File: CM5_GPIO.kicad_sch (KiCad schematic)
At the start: 20 parts, among them J14 JST_SHBM04B-SRSS-TB, J3 Conn_01x03, J7 Micro_SD_Card_Det, J8 THD-20-R, SW1 Right angle Tact button, U18 RT9742GGJ5

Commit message: end of jan 11th
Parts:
- added J2: Conn_02x07_Odd_Even, Connector_PinHeader_2.54mm:PinHeader_2x07_P2.54mm_Vertical, symbol Connector_Generic:Conn_02x07_Odd_Even
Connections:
- net EEPROM_nWP: now also J2.4 (Pin_4)
- net GND: now also J2.1 (Pin_1), J2.11 (Pin_11), J2.13 (Pin_13), J2.3 (Pin_3), J2.5 (Pin_5), J2.7 (Pin_7), J2.9 (Pin_9)
- net PMIC_ENABLE: now also J2.12 (Pin_12)
- net PWR_BUT: now also J2.14 (Pin_14)
- net SYNC_OUT: now also J2.6 (Pin_6)
- net nRPIBOOT: now also J2.2 (Pin_2)
- new net USBOTG: J2.10 (Pin_10)
- no-connect marks 8 -> 20

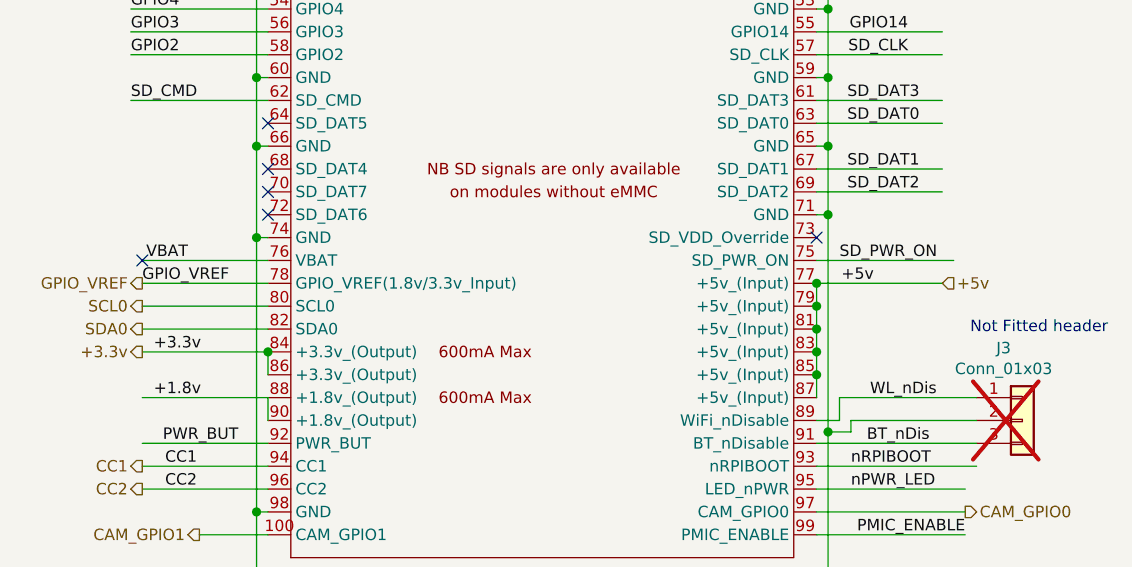
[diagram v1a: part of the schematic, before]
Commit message: Removed ERC errors and M2 connector
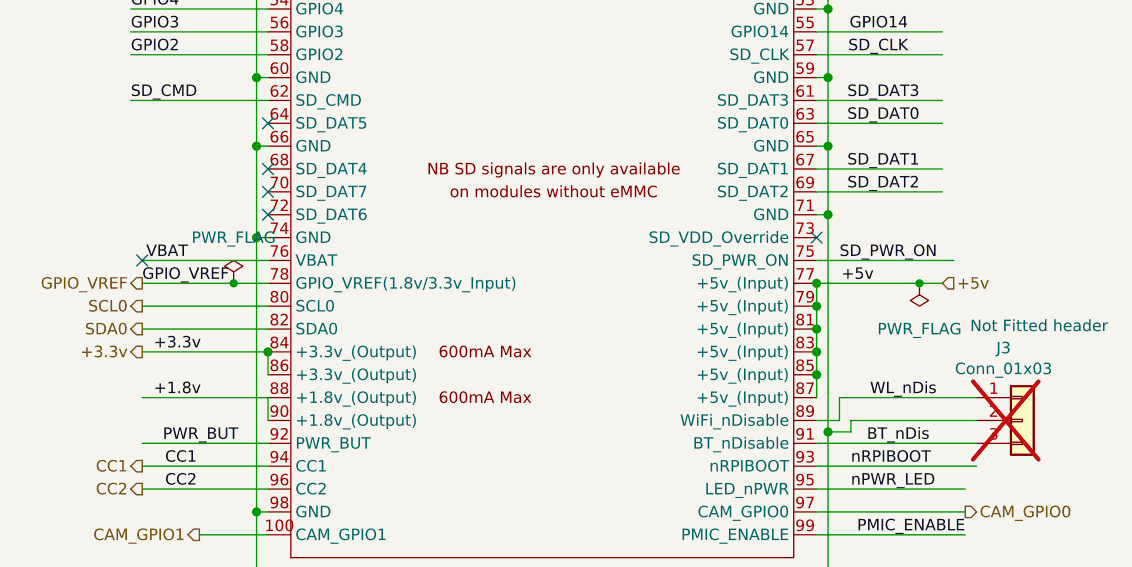
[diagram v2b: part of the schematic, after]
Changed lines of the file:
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@@
 	)
 	(junction
+		(at 35.56 118.11)
+		(diameter 0)
+		(color 0 0 0 0)
+	)
+	(junction
 		(at 100.33 125.73)
 		(diameter 1.016)
@@
 	)
 	(junction
+		(at 111.76 118.11)
+		(diameter 0)
+		(color 0 0 0 0)
+	)
+	(junction
 		(at 149.86 24.13)
 		(diameter 1.016)
@@
 	(wire
 		(pts
-			(xy 100.33 118.11) (xy 114.3 118.11)
+			(xy 100.33 118.11) (xy 111.76 118.11)
 		)
 		(stroke
@@
 	(wire
 		(pts
+			(xy 35.56 118.11) (xy 39.37 118.11)
+		)
+		(stroke
+			(width 0)
+			(type solid)
+		)
+	)
+	(wire
+		(pts
 			(xy 24.13 24.13) (xy 39.37 24.13)
 		)
@@
 	(wire
 		(pts
-			(xy 25.4 118.11) (xy 39.37 118.11)
+			(xy 25.4 118.11) (xy 35.56 118.11)
 		)
 		(stroke
@@
 	(wire
 		(pts
+			(xy 111.76 118.11) (xy 114.3 118.11)
+		)
+		(stroke
+			(width 0)
+			(type solid)
+		)
+	)
+	(wire
+		(pts
 			(xy 160.02 109.22) (xy 156.21 109.22)
 		)
@@
 	)
 	(symbol
+		(lib_id "power:PWR_FLAG")
+		(at 35.56 118.11 0)
+		(unit 1)
+		(exclude_from_sim no)
+		(in_bom yes)
+		(on_board yes)
+		(dnp no)
+		(fields_autoplaced yes)
+		(property "Reference" "#FLG02"
+			(at 35.56 116.205 0)
+			(effects
+				(font
+					(size 1.27 1.27)
+				)
+				(hide yes)
+			)
+		)
+		(property "Value" "PWR_FLAG"
+			(at 35.56 113.03 0)
+			(effects
+				(font
+					(size 1.27 1.27)
+				)
+			)
+		)
+		(property "Footprint" ""
+			(at 35.56 118.11 0)
+			(effects
+				(font
+					(size 1.27 1.27)
+				)
+				(hide yes)
+			)
+		)
+		(property "Datasheet" "~"
+			(at 35.56 118.11 0)
+			(effects
+				(font
+					(size 1.27 1.27)
+				)
+				(hide yes)
+			)
+		)
+		(property "Description" "Special symbol for telling ERC where power comes from"
+			(at 35.56 118.11 0)
+			(effects
+				(font
+					(size 1.27 1.27)
+				)
+				(hide yes)
+			)
+		)
+		(pin "1"
+		)
+		(instances
+			(project ""
+				(path "/e63e39d7-6ac0-4ffd-8aa3-1841a4541b55/00000000-0000-0000-0000-00005cff706a"
+					(reference "#FLG02")
+					(unit 1)
+				)
+			)
+		)
+	)
+	(symbol
 		(lib_id "Device:R")
 		(at 250.19 152.4 0)
@@
 					(unit 1)
 				)
+			)
+		)
+	)
+	(symbol
+		(lib_id "power:PWR_FLAG")
+		(at 111.76 118.11 180)
+		(unit 1)
+		(exclude_from_sim no)
+		(in_bom yes)
+		(on_board yes)
+		(dnp no)
+		(fields_autoplaced yes)
+		(property "Reference" "#FLG01"
+			(at 111.76 120.015 0)
+			(effects
+				(font
+					(size 1.27 1.27)
+				)
+				(hide yes)
+			)
+		)
+		(property "Value" "PWR_FLAG"
+			(at 111.76 123.19 0)
+			(effects
+				(font
+					(size 1.27 1.27)
+				)
+			)
+		)
+		(property "Footprint" ""
+			(at 111.76 118.11 0)
+			(effects
+				(font
+					(size 1.27 1.27)
+				)
+				(hide yes)
+			)
+		)
+		(property "Datasheet" "~"
+			(at 111.76 118.11 0)
+			(effects
+				(font
+					(size 1.27 1.27)
+				)
+				(hide yes)
+			)
+		)
+		(property "Description" "Special symbol for telling ERC where power comes from"
+			(at 111.76 118.11 0)
+			(effects
+				(font
+					(size 1.27 1.27)
+				)
+				(hide yes)
+			)
+		)
+		(pin "1"
+		)
+		(instances
+			(project ""
+				(path "/e63e39d7-6ac0-4ffd-8aa3-1841a4541b55/00000000-0000-0000-0000-00005cff706a"
+					(reference "#FLG01")
+					(unit 1)
+				)
